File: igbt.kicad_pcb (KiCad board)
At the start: 2 copper layers, 160 x 99.7 mm, 38 parts, among them J1 A_Top, J2 A_Bottom, J3 B_Top, J4 B_Bottom, J5 C_Top, J6 C_Bottom, J7 Sense_AC_B, J8 Sense_AC_A, J9 DC_Sense, Q1 IRG4PF50W, Q2 IRG4PF50W, Q3 IRG4PF50W, Q4 IRG4PF50W, Q5 IRG4PF50W, Q6 IRG4PF50W, U1 ACS758xCB-050B-PFF, U2 ACS758xCB-050B-PFF

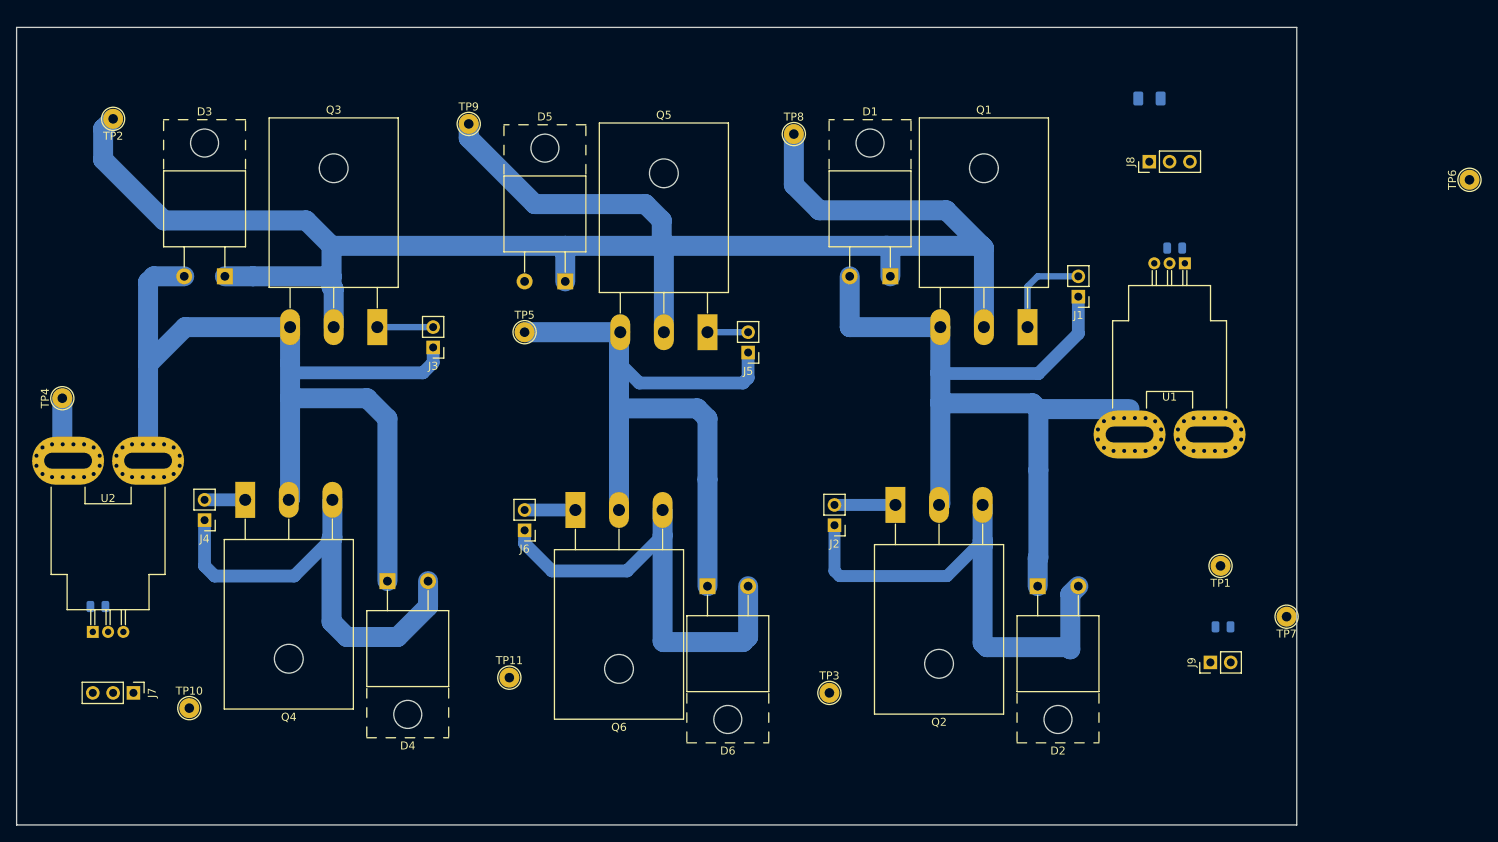
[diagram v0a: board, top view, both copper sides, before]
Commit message: gate pull-down added
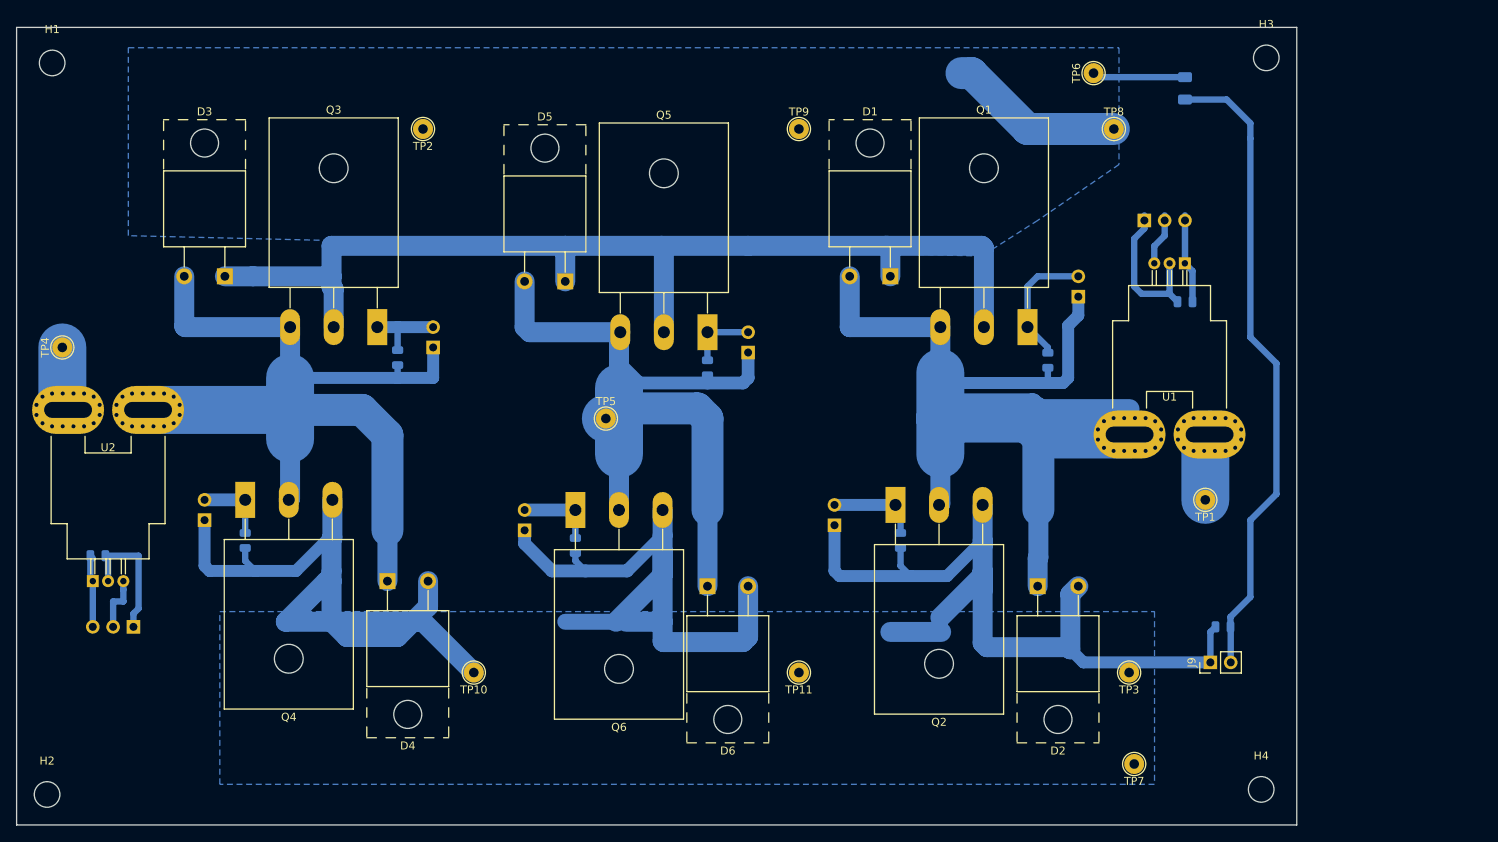
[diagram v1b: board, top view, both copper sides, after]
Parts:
- added H1: MountingHole, MountingHole:MountingHole_3.2mm_M3, F.Cu at (67.9, 50.8)
- added H2: MountingHole, MountingHole:MountingHole_3.2mm_M3, F.Cu at (67.3, 142.2)
- added H3: MountingHole, MountingHole:MountingHole_3.2mm_M3, F.Cu at (219.7, 50.2)
- added H4: MountingHole, MountingHole:MountingHole_3.2mm_M3, F.Cu at (219.1, 141.6)
- added R1: R, Capacitor_SMD:C_0805_2012Metric, B.Cu at (192.4, 88.0)
- added R2: R, Capacitor_SMD:C_0805_2012Metric, B.Cu at (174.0, 110.5)
- added R3: R, Capacitor_SMD:C_0805_2012Metric, B.Cu at (111.1, 87.6)
- added R4: R, Capacitor_SMD:C_0805_2012Metric, B.Cu at (92.1, 110.5)
- added R5: R, Capacitor_SMD:C_0805_2012Metric, B.Cu at (149.9, 88.9)
- added R6: R, Capacitor_SMD:C_0805_2012Metric, B.Cu at (133.3, 111.1)
- J1, J2, J3, J4, J5, J6, J7, J8: moved to B.Cu
- moved TP6 48.8 mm to (198.1, 52.1)
- moved TP9 41.3 mm to (161.3, 59.1)
- moved TP8 40.0 mm to (200.7, 59.1)
- moved TP2 38.8 mm to (114.3, 59.1)
- moved TP3 37.6 mm to (202.6, 127.0), turned to 180 degrees
- moved TP11 36.2 mm to (161.3, 127.0), turned to 180 degrees
- moved TP10 35.8 mm to (120.7, 127.0), turned to 180 degrees
- moved TP7 26.5 mm to (203.2, 138.4)
- moved TP5 14.8 mm to (137.2, 95.2)
- moved TP1 8.47 mm to (212.1, 105.4)
- moved J7 8.25 mm to (78.1, 121.3), turned to 90 degrees
- moved J8 7.37 mm to (204.5, 70.5), turned to 270 degrees
- moved C4 6.83 mm to (209.6, 80.6)
- moved C5 6.35 mm to (73.7, 112.4)
- moved U2 6.35 mm to (73.0, 115.6)
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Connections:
- net Net-(D1-Pad1) renamed /DC_Link
- net Net-(D2-Pad2) renamed /DC_Link_GND
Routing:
- net /DC_Link_GND: track 176.2 -> 282.1 mm
- net /bus_sense: track 0.00 -> 80.5 mm
- net /DC_Link: track 239.7 -> 168.4 mm
- net Net-(D1-Pad2): track 122.6 -> 172.6 mm
- net Net-(C4-Pad2): track 0.00 -> 19.4 mm
- net Net-(D5-Pad2): track 88.1 -> 105.2 mm
- net Net-(C5-Pad1): track 0.00 -> 16.6 mm
- net Net-(C4-Pad1): track 0.00 -> 11.2 mm
- net Net-(C5-Pad2): track 0.00 -> 9.44 mm
- net Net-(D3-Pad2): track 122.9 -> 113.9 mm
- net Net-(TP1-Pad1): track 0.00 -> 8.39 mm
- net Net-(J7-Pad2): track 0.00 -> 6.99 mm
- net Net-(J8-Pad2): track 0.00 -> 6.53 mm
- net Net-(J1-Pad2): track 12.0 -> 16.2 mm
- net Net-(J4-Pad2): track 5.08 -> 9.22 mm
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- added copper zone on B.Cu, net /DC_Link
- added copper zone on B.Cu, net /DC_Link_GND

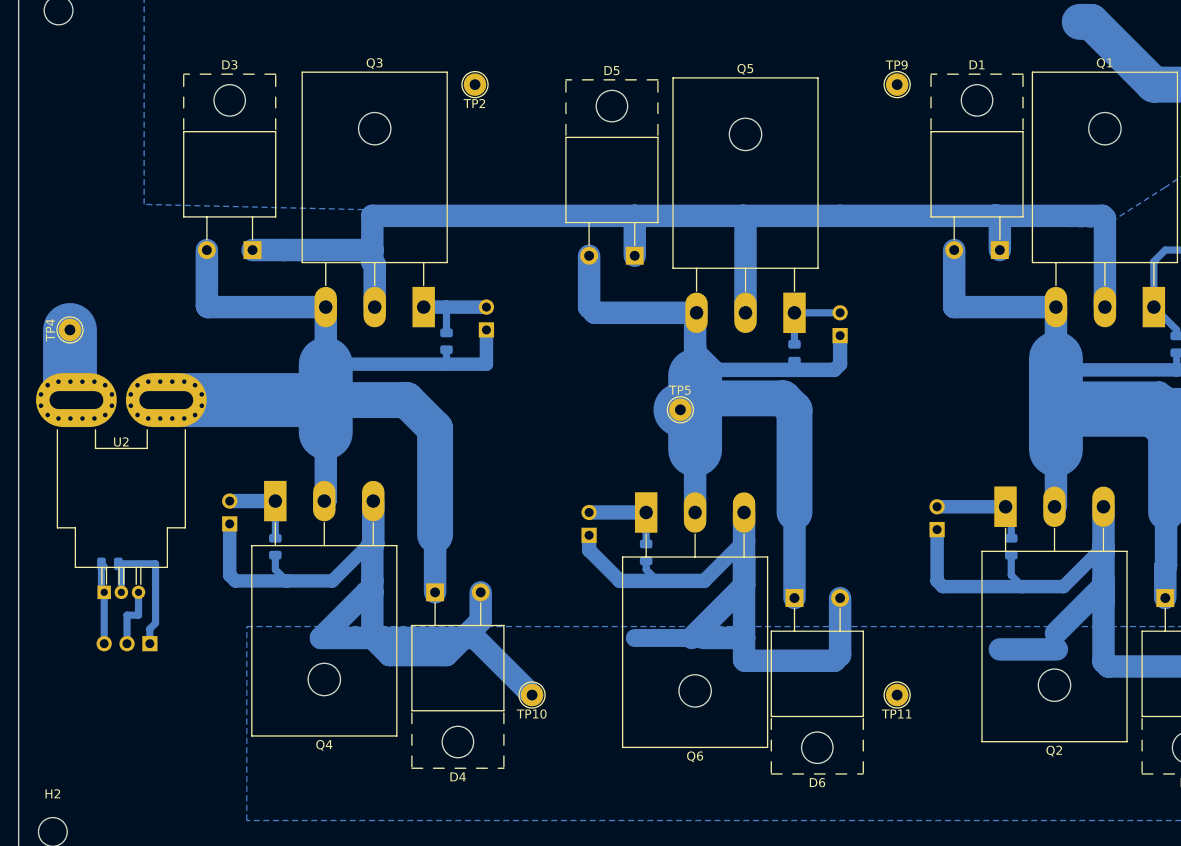
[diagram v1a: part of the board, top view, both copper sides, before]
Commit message: Motor connector added
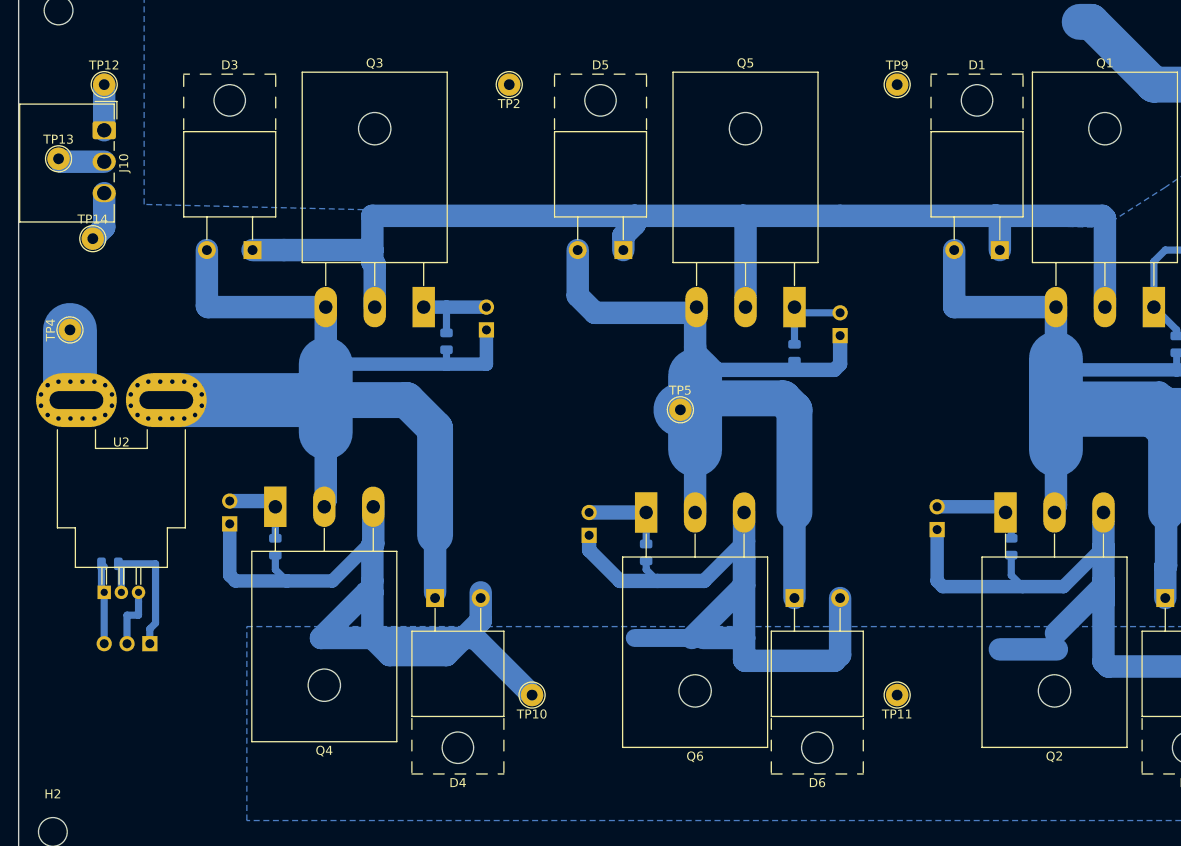
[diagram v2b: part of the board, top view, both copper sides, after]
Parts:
- added J10: Motor, Connector_Wago:Wago_734-163_1x03_P3.50mm_Horizontal, F.Cu at (73.0, 64.1)
- added TP12: MA, TestPoint:TestPoint_THTPad_D2.5mm_Drill1.2mm, F.Cu at (73.0, 59.1)
- added TP13: MB, TestPoint:TestPoint_THTPad_D2.5mm_Drill1.2mm, F.Cu at (67.9, 67.3)
- added TP14: MC, TestPoint:TestPoint_THTPad_D2.5mm_Drill1.2mm, F.Cu at (71.8, 76.2)
- moved TP2 3.81 mm to (118.1, 59.1)
- moved D5 1.42 mm to (130.8, 77.5)
- moved D4 0.64 mm to (109.9, 116.2)
- moved Q2 0.64 mm to (173.4, 106.7)
- moved Q4 0.64 mm to (92.1, 106.0)
- moved Q5 0.64 mm to (149.9, 83.8)
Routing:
- net Net-(J10-Pad3): track 0.00 -> 5.59 mm
- net Net-(J10-Pad2): track 0.00 -> 5.21 mm
- net Net-(J10-Pad1): track 0.00 -> 5.08 mm
- net Net-(D5-Pad2): track 105.2 -> 106.4 mm

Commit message: Pins locked
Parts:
- J9, TP12, TP13, TP14: moved to B.Cu
- moved J1 6.48 mm to (194.9, 86.4)
- moved TP14 1.91 mm to (71.8, 78.1)
- moved J2 1.42 mm to (167.0, 109.2)
- moved R1 1.27 mm to (191.1, 88.0)
- moved J4 1.27 mm to (87.0, 109.2)
- moved J5 0.64 mm to (154.9, 86.4)
- moved Q4 0.64 mm to (92.1, 106.7)
- turned J9 to 270 degrees
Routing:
- net Net-(D1-Pad2): track 172.6 -> 164.9 mm
- net Net-(J1-Pad2): track 16.2 -> 8.81 mm
- net /DC_Link_GND: track 282.1 -> 279.0 mm
- net Net-(J10-Pad3): track 5.59 -> 7.50 mm
- net Net-(J2-Pad2): track 11.4 -> 10.1 mm
- net Net-(D5-Pad2): track 106.4 -> 107.3 mm
- net Net-(J5-Pad2): track 8.59 -> 9.22 mm

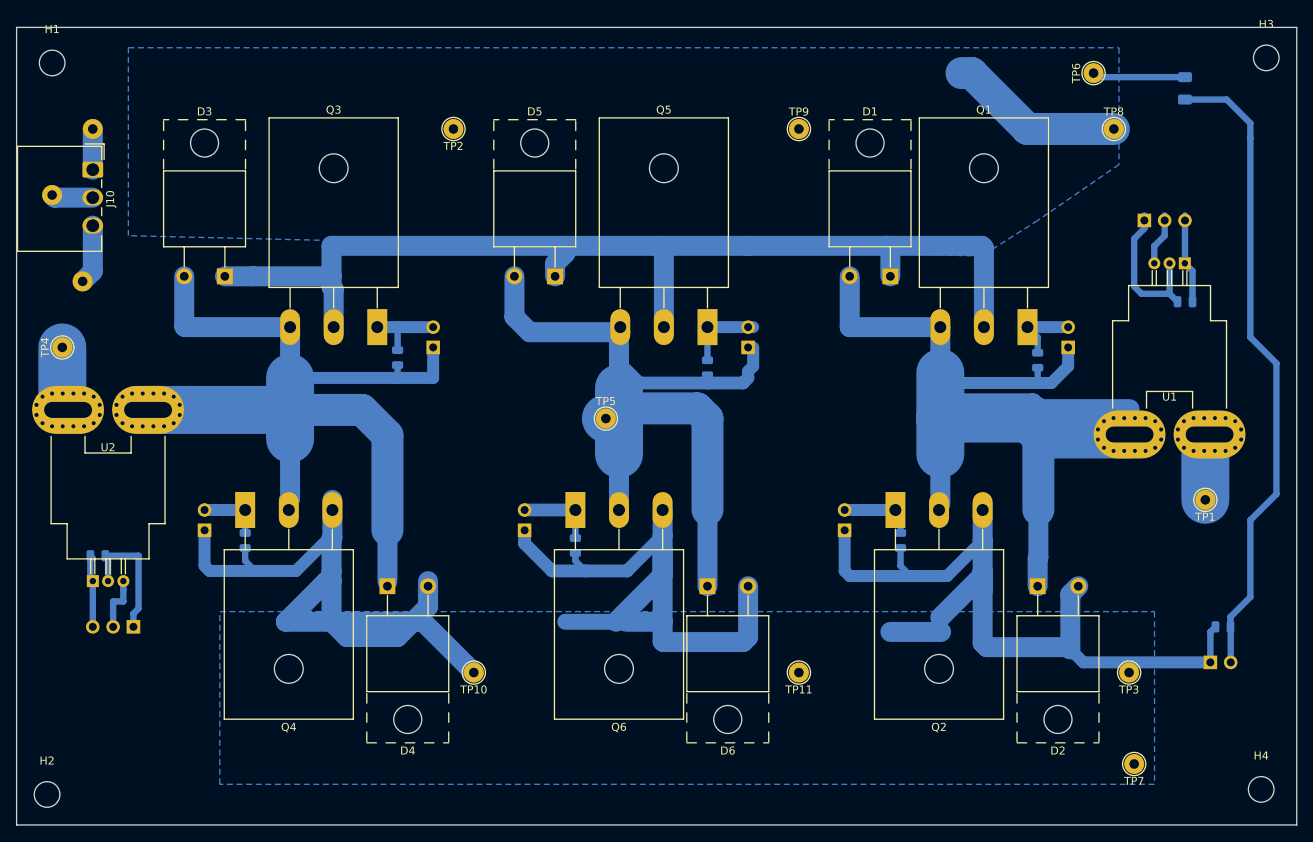
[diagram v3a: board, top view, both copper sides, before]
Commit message: mounting holes 5mm from edges
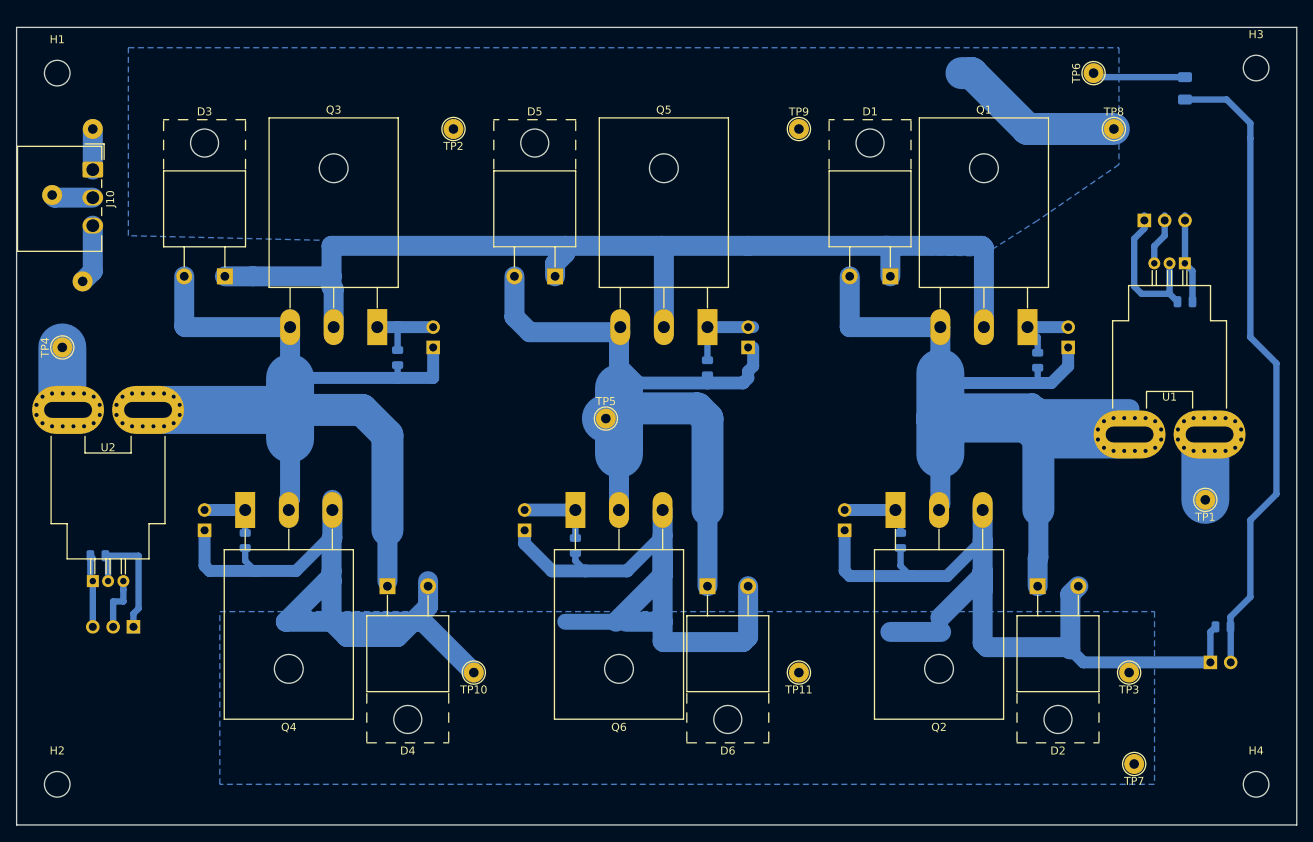
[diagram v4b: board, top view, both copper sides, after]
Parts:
- moved H3 1.80 mm to (218.4, 51.4)
- moved H2 1.80 mm to (68.6, 141.0)
- moved H1 1.42 mm to (68.6, 52.1)
- moved H4 0.90 mm to (218.4, 141.0)
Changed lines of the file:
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@@
   (general
     (thickness 1.6)
-    (drawings 24)
+    (drawings 25)
     (tracks 232)
     (zones 0)
@@
   )
   (module MountingHole:MountingHole_3.2mm_M3 (layer F.Cu)
-    (at 67.31 142.24)
+    (at 68.58 140.97)
     (descr "Mounting Hole 3.2mm, no annular, M3")
     (tags "mounting hole 3.2mm no annular m3")
@@
   )
   (module MountingHole:MountingHole_3.2mm_M3 (layer F.Cu)
-    (at 219.71 50.165)
+    (at 218.44 51.435)
     (descr "Mounting Hole 3.2mm, no annular, M3")
     (tags "mounting hole 3.2mm no annular m3")
@@
   )
   (module MountingHole:MountingHole_3.2mm_M3 (layer F.Cu)
-    (at 219.075 141.605)
+    (at 218.44 140.97)
     (descr "Mounting Hole 3.2mm, no annular, M3")
     (tags "mounting hole 3.2mm no annular m3")
@@
   )
   (module MountingHole:MountingHole_3.2mm_M3 (layer F.Cu)
-    (at 67.945 50.8)
+    (at 68.58 52.07)
     (descr "Mounting Hole 3.2mm, no annular, M3")
     (tags "mounting hole 3.2mm no annular m3")
@@
     )
   )
+  (dimension 160.02 (width 0.3) (layer Dwgs.User)
+    (gr_text "160,020 mm" (at 143.51 38.54) (layer Dwgs.User)
+      (effects (font (size 1.5 1.5) (thickness 0.3)))
+    )
+    (feature1 (pts (xy 223.52 46.355) (xy 223.52 40.053579)))
+    (feature2 (pts (xy 63.5 46.355) (xy 63.5 40.053579)))
+    (crossbar (pts (xy 63.5 40.64) (xy 223.52 40.64)))
+    (arrow1a (pts (xy 223.52 40.64) (xy 222.393496 41.226421)))
+    (arrow1b (pts (xy 223.52 40.64) (xy 222.393496 40.053579)))
+    (arrow2a (pts (xy 63.5 40.64) (xy 64.626504 41.226421)))
+    (arrow2b (pts (xy 63.5 40.64) (xy 64.626504 40.053579)))
+  )
+  (gr_line (start 68.58 145.415) (end 68.58 45.085) (layer Dwgs.User) (width 0.2))
   (dimension 40.005 (width 0.3) (layer Dwgs.User)
     (gr_text "40,005 mm" (at 147.0025 100.135) (layer Dwgs.User)
@@
   (gr_line (start 223.52 46.355) (end 223.52 146.05) (layer Edge.Cuts) (width 0.15))
   (gr_line (start 63.5 46.355) (end 223.52 46.355) (layer Edge.Cuts) (width 0.15))
-  (dimension 160.02 (width 0.3) (layer Dwgs.User)
-    (gr_text "160,020 mm" (at 143.51 38.54) (layer Dwgs.User)
+  (dimension 99.695 (width 0.3) (layer Dwgs.User)
+    (gr_text "99,695 mm" (at 52.51 96.205741 -90) (layer Dwgs.User)
       (effects (font (size 1.5 1.5) (thickness 0.3)))
     )
-    (feature1 (pts (xy 223.52 46.355) (xy 223.52 40.053579)))
-    (feature2 (pts (xy 63.5 46.355) (xy 63.5 40.053579)))
-    (crossbar (pts (xy 63.5 40.64) (xy 223.52 40.64)))
-    (arrow1a (pts (xy 223.52 40.64) (xy 222.393496 41.226421)))
-    (arrow1b (pts (xy 223.52 40.64) (xy 222.393496 40.053579)))
-    (arrow2a (pts (xy 63.5 40.64) (xy 64.626504 41.226421)))
-    (arrow2b (pts (xy 63.5 40.64) (xy 64.626504 40.053579)))
-  )
-  (dimension 99.695 (width 0.3) (layer Dwgs.User)
-    (gr_text "99,695 mm" (at 52.51 37.773196 -90) (layer Dwgs.User)
-      (effects (font (size 1.5 1.5) (thickness 0.3)))
-    )
-    (feature1 (pts (xy 63.5 87.620696) (xy 54.023579 87.620696)))
-    (feature2 (pts (xy 63.5 -12.074304) (xy 54.023579 -12.074304)))
-    (crossbar (pts (xy 54.61 -12.074304) (xy 54.61 87.620696)))
-    (arrow1a (pts (xy 54.61 87.620696) (xy 55.196421 86.494192)))
-    (arrow1b (pts (xy 54.61 87.620696) (xy 54.023579 86.494192)))
-    (arrow2a (pts (xy 54.61 -12.074304) (xy 55.196421 -10.9478)))
-    (arrow2b (pts (xy 54.61 -12.074304) (xy 54.023579 -10.9478)))
+    (feature1 (pts (xy 63.5 146.053241) (xy 54.023579 146.053241)))
+    (feature2 (pts (xy 63.5 46.358241) (xy 54.023579 46.358241)))
+    (crossbar (pts (xy 54.61 46.358241) (xy 54.61 146.053241)))
+    (arrow1a (pts (xy 54.61 146.053241) (xy 55.196421 144.926737)))
+    (arrow1b (pts (xy 54.61 146.053241) (xy 54.023579 144.926737)))
+    (arrow2a (pts (xy 54.61 46.358241) (xy 55.196421 47.484745)))
+    (arrow2b (pts (xy 54.61 46.358241) (xy 54.023579 47.484745)))
   )
   (segment (start 178.965 83.82) (end 167.64 83.82) (width 2.5) (layer B.Cu) (net 1))
